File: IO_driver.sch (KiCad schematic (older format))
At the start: 9 parts, among them J2001 BNC, U2001 74LVC2T45DC

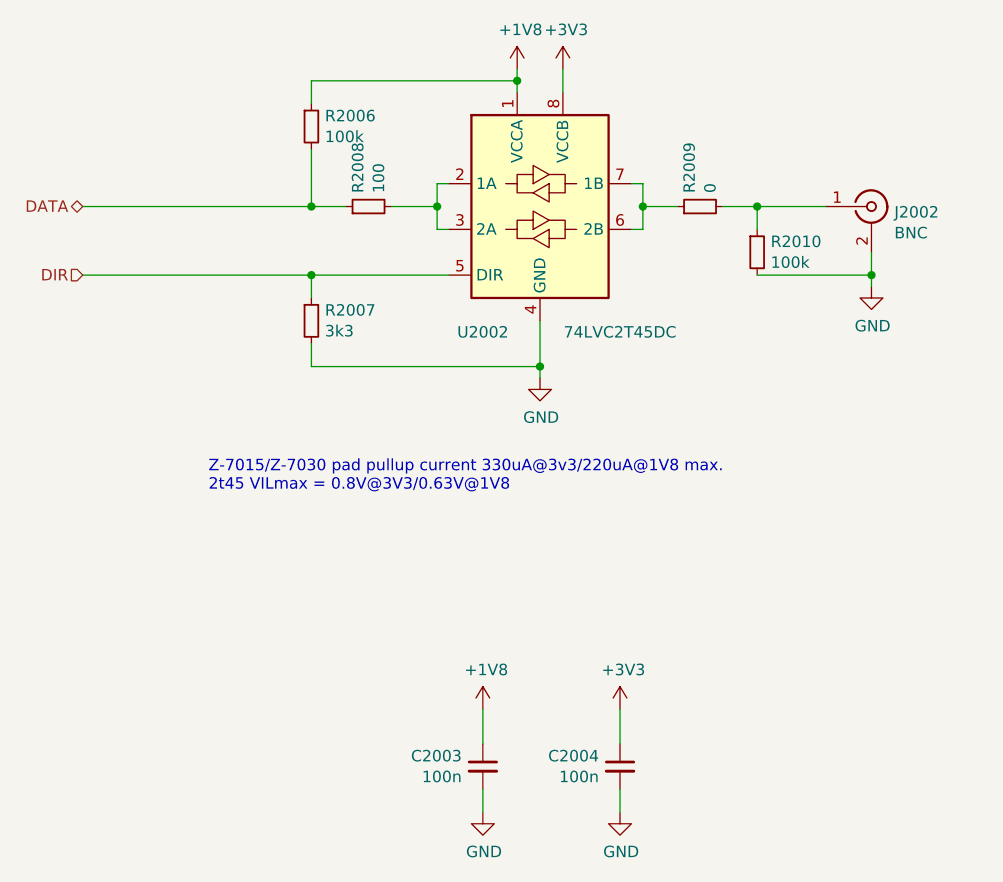
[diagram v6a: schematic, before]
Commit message: updated cap footprint
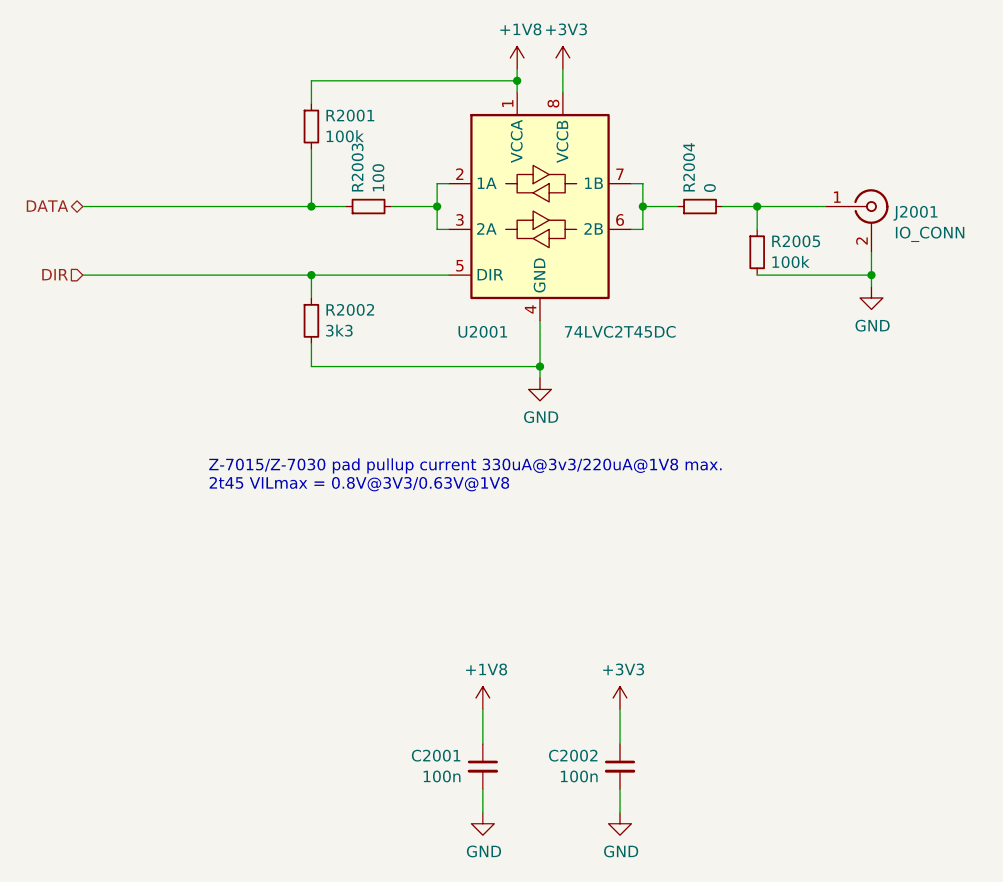
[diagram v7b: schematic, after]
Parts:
- J2001: value BNC -> IO_CONN; Manufacturer Molex -> LEMO; Part 0731713150 -> (none)
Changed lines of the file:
@@
 $Descr A4 11693 8268
 encoding utf-8
-Sheet 18 21
+Sheet 15 21
 Title ""
 Date ""
@@
 AR Path="/60E70F2C/626DBAF0/60F26603" Ref="R94"  Part="1"
 AR Path="/60E70F2C/62739E15/60F26603" Ref="R2009"  Part="1"
-F 0 "R2009" H 5259 1896 50  0000 L CNN
+F 0 "R2004" H 5259 1896 50  0000 L CNN
 F 1 "0" H 5259 1805 50  0000 L CNN
 F 2 "Resistor_SMD:R_0603_1608Metric" H 5200 1850 50  0001 C CNN
@@
 AR Path="/60E70F2C/626DBAF0/60F26C82" Ref="R93"  Part="1"
 AR Path="/60E70F2C/62739E15/60F26C82" Ref="R2008"  Part="1"
-F 0 "R2008" H 3809 1896 50  0000 L CNN
+F 0 "R2003" H 3809 1896 50  0000 L CNN
 F 1 "100" H 3809 1805 50  0000 L CNN
 F 2 "Resistor_SMD:R_0603_1608Metric" H 3750 1850 50  0001 C CNN
@@
 AR Path="/60E70F2C/626DBAF0/60F2A5CB" Ref="C106"  Part="1"
 AR Path="/60E70F2C/62739E15/60F2A5CB" Ref="C2003"  Part="1"
-F 0 "C2003" H 4342 4346 50  0000 L CNN
+F 0 "C2001" H 4342 4346 50  0000 L CNN
 F 1 "100n" H 4342 4255 50  0000 L CNN
 F 2 "Capacitor_SMD:C_0402_1005Metric" H 4250 4300 50  0001 C CNN
@@
 AR Path="/60E70F2C/626DBAF0/60F2C544" Ref="C107"  Part="1"
 AR Path="/60E70F2C/62739E15/60F2C544" Ref="C2004"  Part="1"
-F 0 "C2004" H 4942 4346 50  0000 L CNN
+F 0 "C2002" H 4942 4346 50  0000 L CNN
 F 1 "100n" H 4942 4255 50  0000 L CNN
 F 2 "Capacitor_SMD:C_0402_1005Metric" H 4850 4300 50  0001 C CNN
@@
 AR Path="/60E70F2C/626DBAF0/60E51E93" Ref="J5"  Part="1"
 AR Path="/60E70F2C/62739E15/60E51E93" Ref="J2002"  Part="1"
-F 0 "J2002" H 6050 1825 50  0000 L CNN
-F 1 "BNC" H 6050 1734 50  0000 L CNN
+F 0 "J2001" H 6050 1825 50  0000 L CNN
+F 1 "IO_CONN" H 6050 1734 50  0000 L CNN
 F 2 "proj_footprints:LEMO+SMA" H 5950 1850 50  0001 C CNN
 F 3 " ~" H 5950 1850 50  0001 C CNN
-F 4 "0731713150" H 5950 1850 50  0001 C CNN "Part"
-F 5 "Molex" H 5950 1850 50  0001 C CNN "Manufacturer"
+F 4 "" H 5950 1850 50  0001 C CNN "Part"
+F 5 "LEMO" H 5950 1850 50  0001 C CNN "Manufacturer"
 	1    5950 1850
 	1    0    0    -1
@@
 AR Path="/60E70F2C/626DBAF0/60F05839" Ref="R95"  Part="1"
 AR Path="/60E70F2C/62739E15/60F05839" Ref="R2010"  Part="1"
-F 0 "R2010" H 5509 2096 50  0000 L CNN
+F 0 "R2005" H 5509 2096 50  0000 L CNN
 F 1 "100k" H 5509 2005 50  0000 L CNN
 F 2 "Resistor_SMD:R_0603_1608Metric" H 5450 2050 50  0001 C CNN
@@
 AR Path="/60E70F2C/626DBAF0/60E41AAA" Ref="U22"  Part="1"
 AR Path="/60E70F2C/62739E15/60E41AAA" Ref="U2002"  Part="1"
-F 0 "U2002" H 4250 1300 50  0000 C CNN
+F 0 "U2001" H 4250 1300 50  0000 C CNN
 F 1 "74LVC2T45DC" H 4850 1300 50  0000 C CNN
 F 2 "Package_SO:VSSOP-8_2.3x2mm_P0.5mm" H 4500 1000 50  0001 C CNN
@@
 AR Path="/60E70F2C/626DBAF0/60E4921E" Ref="R92"  Part="1"
 AR Path="/60E70F2C/62739E15/60E4921E" Ref="R2007"  Part="1"
-F 0 "R2007" H 3559 2396 50  0000 L CNN
+F 0 "R2002" H 3559 2396 50  0000 L CNN
 F 1 "3k3" H 3559 2305 50  0000 L CNN
 F 2 "Resistor_SMD:R_0603_1608Metric" H 3500 2350 50  0001 C CNN
@@
 AR Path="/60E70F2C/626DBAF0/60E49E8E" Ref="R91"  Part="1"
 AR Path="/60E70F2C/62739E15/60E49E8E" Ref="R2006"  Part="1"
-F 0 "R2006" H 3559 1546 50  0000 L CNN
+F 0 "R2001" H 3559 1546 50  0000 L CNN
 F 1 "100k" H 3559 1455 50  0000 L CNN
 F 2 "Resistor_SMD:R_0603_1608Metric" H 3500 1500 50  0001 C CNN
